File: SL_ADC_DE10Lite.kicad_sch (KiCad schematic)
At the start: 22 parts, among them J1 DE10Lite header, J2 Conn_02x08_Odd_Even, J3 Digital ground header, J4 Analog header, J5 Power header

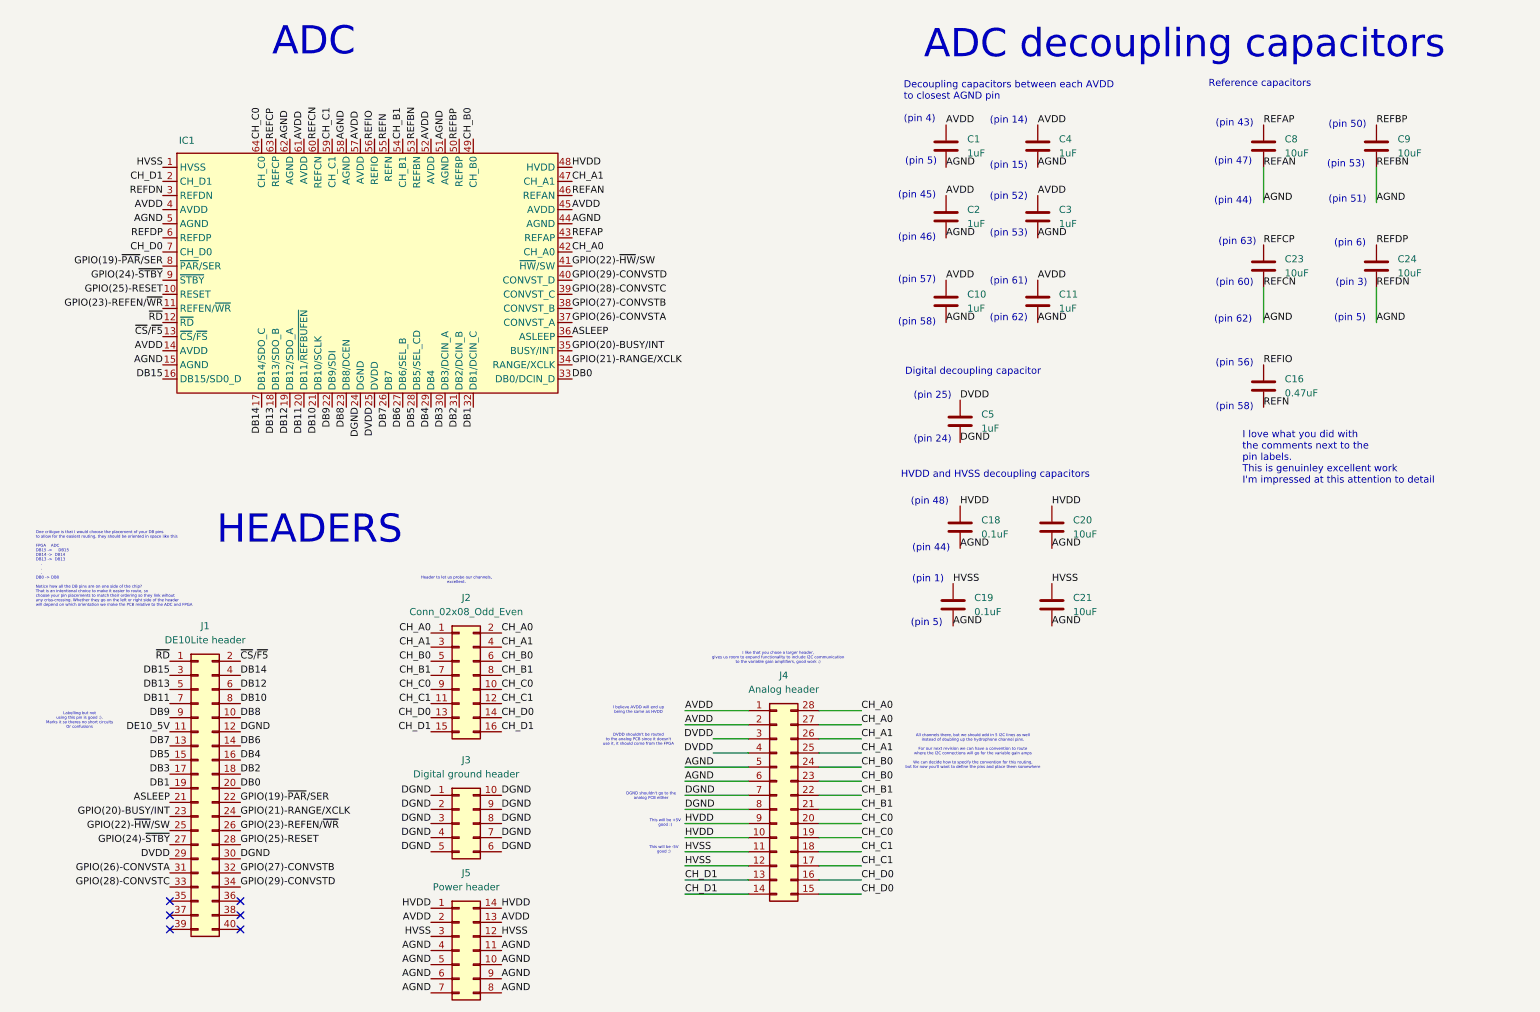
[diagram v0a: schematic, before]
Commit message: Add De10lite dimensions and routes
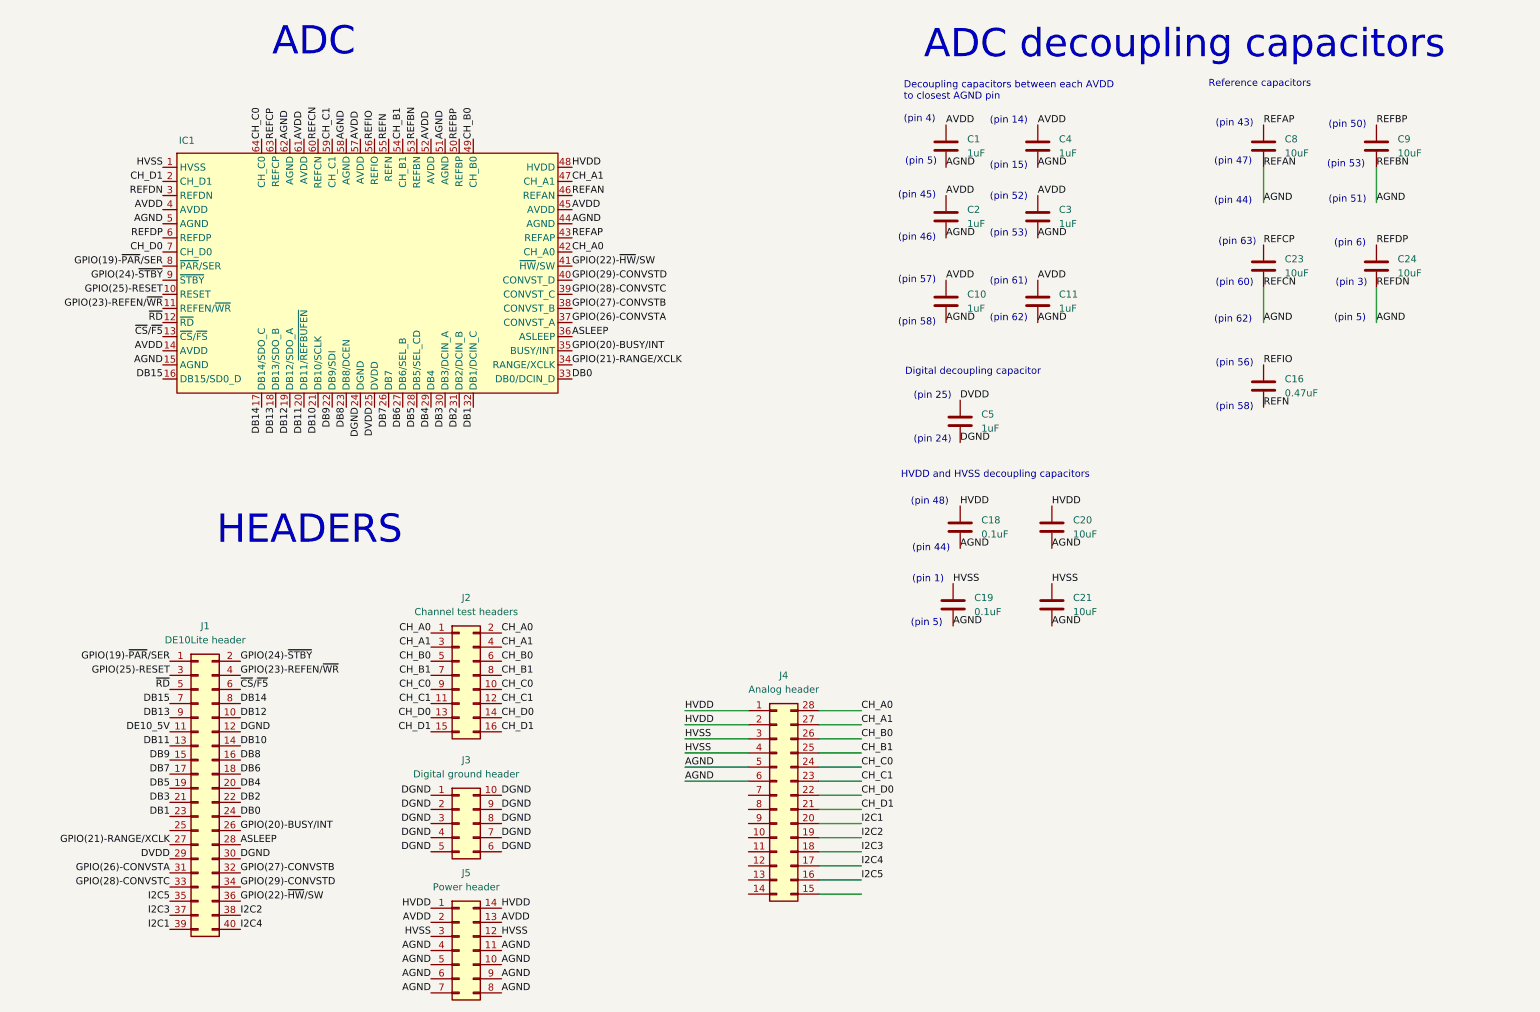
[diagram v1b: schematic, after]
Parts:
- J2: value Conn_02x08_Odd_Even -> Channel test headers
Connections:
- net AGND: now also IC1.51 (AGND)
- net ASLEEP: now also J1.28 (Pin_28); no longer J1.21 (Pin_21)
- net AVDD: no longer J4.1 (Pin_1), J4.2 (Pin_2)
- net CH_A0: no longer J4.27 (Pin_27)
- net CH_A1: now also J4.27 (Pin_27); no longer J4.25 (Pin_25), J4.26 (Pin_26)
- net CH_B0: now also J4.26 (Pin_26); no longer J4.23 (Pin_23), J4.24 (Pin_24)
- net CH_B1: now also J4.25 (Pin_25); no longer J4.21 (Pin_21), J4.22 (Pin_22)
- net CH_C0: now also J4.24 (Pin_24); no longer J4.19 (Pin_19), J4.20 (Pin_20)
- net CH_C1: now also J4.23 (Pin_23); no longer J4.17 (Pin_17), J4.18 (Pin_18)
- net CH_D0: now also J4.22 (Pin_22); no longer J4.15 (Pin_15), J4.16 (Pin_16)
- net CH_D1: now also J4.21 (Pin_21); no longer J4.13 (Pin_13), J4.14 (Pin_14)
- net DB0: now also J1.24 (Pin_24); no longer J1.20 (Pin_20)
- net DB1: now also J1.23 (Pin_23); no longer J1.19 (Pin_19)
- net DB10: now also J1.14 (Pin_14); no longer J1.8 (Pin_8)
- net DB11: now also J1.13 (Pin_13); no longer J1.7 (Pin_7)
- net DB12: now also J1.10 (Pin_10); no longer J1.6 (Pin_6)
- net DB13: now also J1.9 (Pin_9); no longer J1.5 (Pin_5)
- net DB14: now also J1.8 (Pin_8); no longer J1.4 (Pin_4)
- net DB15: now also J1.7 (Pin_7); no longer J1.3 (Pin_3)
- net DB2: now also J1.22 (Pin_22); no longer J1.18 (Pin_18)
- net DB3: now also J1.21 (Pin_21); no longer J1.17 (Pin_17)
- net DB4: now also J1.20 (Pin_20); no longer J1.16 (Pin_16)
- net DB5: now also J1.19 (Pin_19); no longer J1.15 (Pin_15)
- net DB6: now also J1.18 (Pin_18); no longer J1.14 (Pin_14)
- net DB7: now also J1.17 (Pin_17); no longer J1.13 (Pin_13)
- net DB8: now also J1.16 (Pin_16); no longer J1.10 (Pin_10)
- net DB9: now also J1.15 (Pin_15); no longer J1.9 (Pin_9)
- net DGND: no longer J4.7 (Pin_7), J4.8 (Pin_8)
- net DVDD: no longer J4.3 (Pin_3), J4.4 (Pin_4)
- net GPIO(19)-~{PAR}/SER: now also J1.1 (Pin_1); no longer J1.22 (Pin_22)
- net GPIO(20)-BUSY/INT: now also J1.26 (Pin_26); no longer J1.23 (Pin_23)
- net GPIO(21)-RANGE/XCLK: now also J1.27 (Pin_27); no longer J1.24 (Pin_24)
- net GPIO(22)-~{HW}/SW: now also J1.36 (Pin_36); no longer J1.25 (Pin_25)
- net GPIO(23)-REFEN/~{WR}: now also J1.4 (Pin_4); no longer J1.26 (Pin_26)
- net GPIO(24)-~{STBY}: now also J1.2 (Pin_2); no longer J1.27 (Pin_27)
- net GPIO(25)-RESET: now also J1.3 (Pin_3); no longer J1.28 (Pin_28)
- net HVDD: now also J4.1 (Pin_1), J4.2 (Pin_2); no longer J4.10 (Pin_10), J4.9 (Pin_9)
- net HVSS: now also J4.3 (Pin_3), J4.4 (Pin_4); no longer J4.11 (Pin_11), J4.12 (Pin_12)
- net ~{CS}/~{F5}: now also J1.6 (Pin_6); no longer J1.2 (Pin_2)
- net ~{RD}: now also J1.5 (Pin_5); no longer J1.1 (Pin_1)
- net I2C5: now reaches J1.35 (Pin_35)
- net I2C5: now also J4.16 (Pin_16)
- net I2C3: now reaches J1.37 (Pin_37)
- net I2C3: now also J4.18 (Pin_18)
- net I2C2: now reaches J1.38 (Pin_38)
- net I2C2: now also J4.19 (Pin_19)
- net I2C1: now reaches J1.39 (Pin_39)
- net I2C1: now also J4.20 (Pin_20)
- net I2C4: now reaches J1.40 (Pin_40)
- net I2C4: now also J4.17 (Pin_17)
- no-connect marks 6 -> 0
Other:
- note removed: "All channels there, but we should add in 5 I2C lines as well instead of doubling up the hydrophone channel pins. For our next revision we can have a convention to route where the I2C connections will go for the variable gain amps We can decide how to specify the convention for this routing, but for now you'll want to define the pins and place them somewhere"
- note removed: "DGND shouldn't go to the analog PCB either"
- note removed: "DVDD shouldn't be routed to the analog PCB since it doesn't use it, it should come from the FPGA"
- note removed: "Header to let us probe our channels, excellent."
- note removed: "I believe AVDD will end up being the same as HVDD"
- note removed: "I like that you chose a larger header, gives us room to expand functionality to include I2C communication to the variable gain amplifiers, good work :)"
- note removed: "I love what you did with the comments next to the pin labels. This is genuinley excellent work I'm impressed at this attention to detail"
- note removed: "Labelling but not using this pin is good :). Marks it so theres no short circuits Or confusions"
- note removed: "One critique is that I would choose the placement of your DB pins to allow for the easiest routing, they should be oriented in space like this FPGA ADC DB15 -> DB15 DB14 -> DB14 DB13 -> DB13 . . . DB0 -> DB0 Notice how all the DB pins are on one side of the chip? That is an intentional choice to make it easier to route, so choose your pin placements to match their ordering so they link wihout any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"
- note removed: "This will be +5V good :)"
- note removed: "This will be -5V good :)"

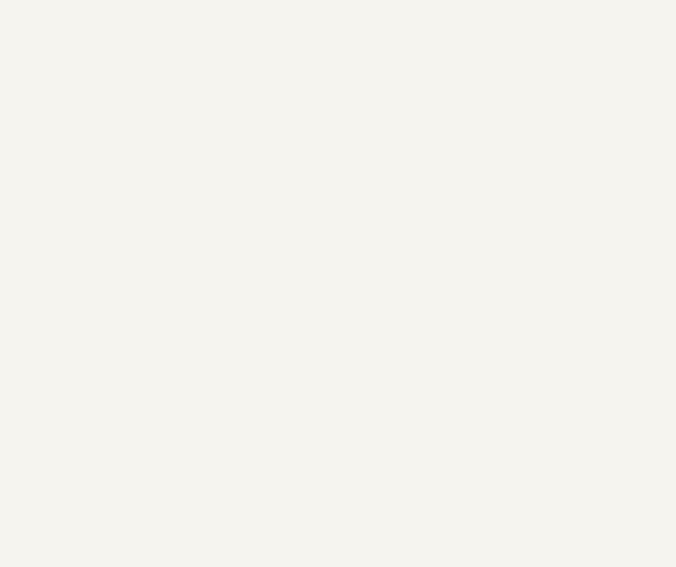
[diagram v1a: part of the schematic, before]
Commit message: Define separate AGND and DGND copper fill
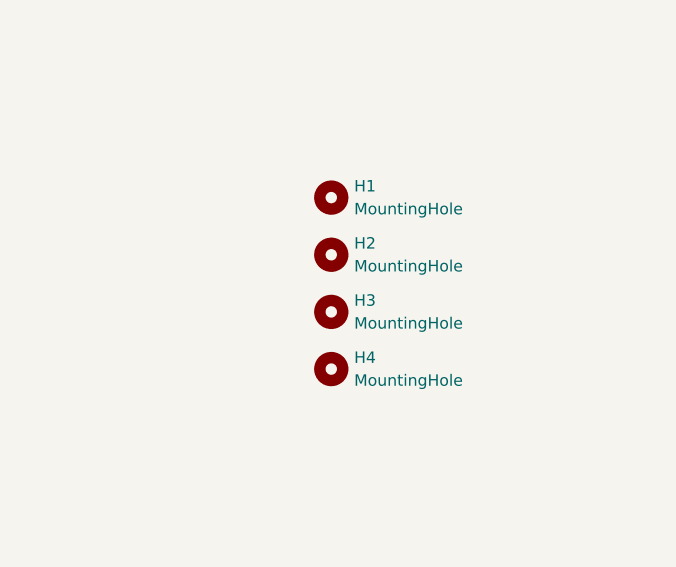
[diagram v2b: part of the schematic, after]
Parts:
- added H1, H2, H3, H4: MountingHole, MountingHole:MountingHole_2.5mm, symbol Mechanical:MountingHole

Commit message: Recent changes
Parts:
- removed J2: Channel test headers, Connector_PinHeader_2.54mm:PinHeader_2x08_P2.54mm_Vertical, symbol Connector_Generic:Conn_02x08_Odd_Even
- removed J3: Digital ground header, Connector_PinHeader_2.54mm:PinHeader_2x05_P2.54mm_Vertical, symbol Connector_Generic:Conn_02x05_Counter_Clockwise
- removed J5: Power header, symbol Connector_Generic:Conn_02x07_Counter_Clockwise
- added J6: Testing header, Connector_PinHeader_2.54mm:PinHeader_2x14_P2.54mm_Horizontal, symbol Connector_Generic:Conn_02x14_Counter_Clockwise
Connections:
- net AGND: now also J6.15 (Pin_15), J6.16 (Pin_16), J6.17 (Pin_17), J6.18 (Pin_18), J6.19 (Pin_19), J6.20 (Pin_20)
- net AVDD: now also J6.25 (Pin_25), J6.26 (Pin_26)
- net CH_A0: now also J6.1 (Pin_1)
- net CH_A1: now also J6.2 (Pin_2)
- net CH_B0: now also J6.3 (Pin_3)
- net CH_B1: now also J6.4 (Pin_4)
- net CH_C0: now also J6.5 (Pin_5)
- net CH_C1: now also J6.6 (Pin_6)
- net CH_D0: now also J6.7 (Pin_7)
- net CH_D1: now also J6.8 (Pin_8)
- net DGND: now also J6.10 (Pin_10), J6.11 (Pin_11), J6.12 (Pin_12), J6.13 (Pin_13), J6.14 (Pin_14), J6.21 (Pin_21), J6.22 (Pin_22), J6.9 (Pin_9)
- net HVDD: now also J6.27 (Pin_27), J6.28 (Pin_28)
- net HVSS: now also J6.23 (Pin_23), J6.24 (Pin_24)
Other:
- moved on the sheet: J4

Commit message: Updated version
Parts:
- removed J4: Analog header, Connector_PinHeader_2.54mm:PinHeader_2x14_P2.54mm_Vertical, symbol Connector_Generic:Conn_02x14_Counter_Clockwise
- removed J6: Testing header, Connector_PinHeader_2.54mm:PinHeader_2x14_P2.54mm_Horizontal, symbol Connector_Generic:Conn_02x14_Counter_Clockwise
- added J2: Conn_02x14_Odd_Even, Connector_PinHeader_2.54mm:PinHeader_2x14_P2.54mm_Vertical, symbol Connector_Generic:Conn_02x14_Odd_Even
- added J3: Conn_02x04_Odd_Even, Connector_PinHeader_2.54mm:PinHeader_2x04_P2.54mm_Horizontal, symbol Connector_Generic:Conn_02x04_Odd_Even
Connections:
- net AGND: now also J2.11 (Pin_11), J2.13 (Pin_13), J2.15 (Pin_15), J2.17 (Pin_17), J2.19 (Pin_19), J2.5 (Pin_5), J2.7 (Pin_7), J2.9 (Pin_9)
- net CH_A0: now also J2.14 (Pin_14), J3.2 (Pin_2)
- net CH_A1: now also J2.16 (Pin_16), J3.4 (Pin_4)
- net CH_B0: now also J2.18 (Pin_18), J3.6 (Pin_6)
- net CH_B1: now also J2.20 (Pin_20), J3.8 (Pin_8)
- net CH_C0: now also J2.22 (Pin_22), J3.7 (Pin_7)
- net CH_C1: now also J2.24 (Pin_24), J3.5 (Pin_5)
- net CH_D0: now also J2.26 (Pin_26), J3.3 (Pin_3)
- net CH_D1: now also J2.28 (Pin_28), J3.1 (Pin_1)
- net DVDD: now also J2.1 (Pin_1), J2.3 (Pin_3)
- net HVDD: now also J2.25 (Pin_25), J2.27 (Pin_27)
- net HVSS: now also J2.21 (Pin_21), J2.23 (Pin_23)
- net I2C1: now also J2.2 (Pin_2)
- net I2C2: now also J2.4 (Pin_4)
- net I2C3: now also J2.6 (Pin_6)
- net I2C4: now also J2.8 (Pin_8)
- net I2C5: now also J2.10 (Pin_10)
